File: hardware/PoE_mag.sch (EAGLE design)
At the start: 124 parts, among them IC1 LD1117V33, IC10 74LVC1T45SOT23-HAND, IC11 PCA9517A, IC2 LD1117V33, IC3 DS1338, IC4 ATMEGA1284, IC5 TSR 1-2450, IC6 MCP2200, IC7 74LVC1T45SOT23-HAND, IC8 74LVC1T45SOT23-HAND, IC9 74LVC1T45SOT23-HAND, Q1 BSS138, Q2 BUK98150-55A, X1 PWR, X2 JTAG, X3 USB, X4 MICRO-SD-SOCKETHIROSE-DM3D, X5 CONN-SMATHD, X6 UFL, X7 22-23-2021, X8 RJ45, X9 RJ11, Y1 32k768, Y2 16MHz, Y3 12MHz

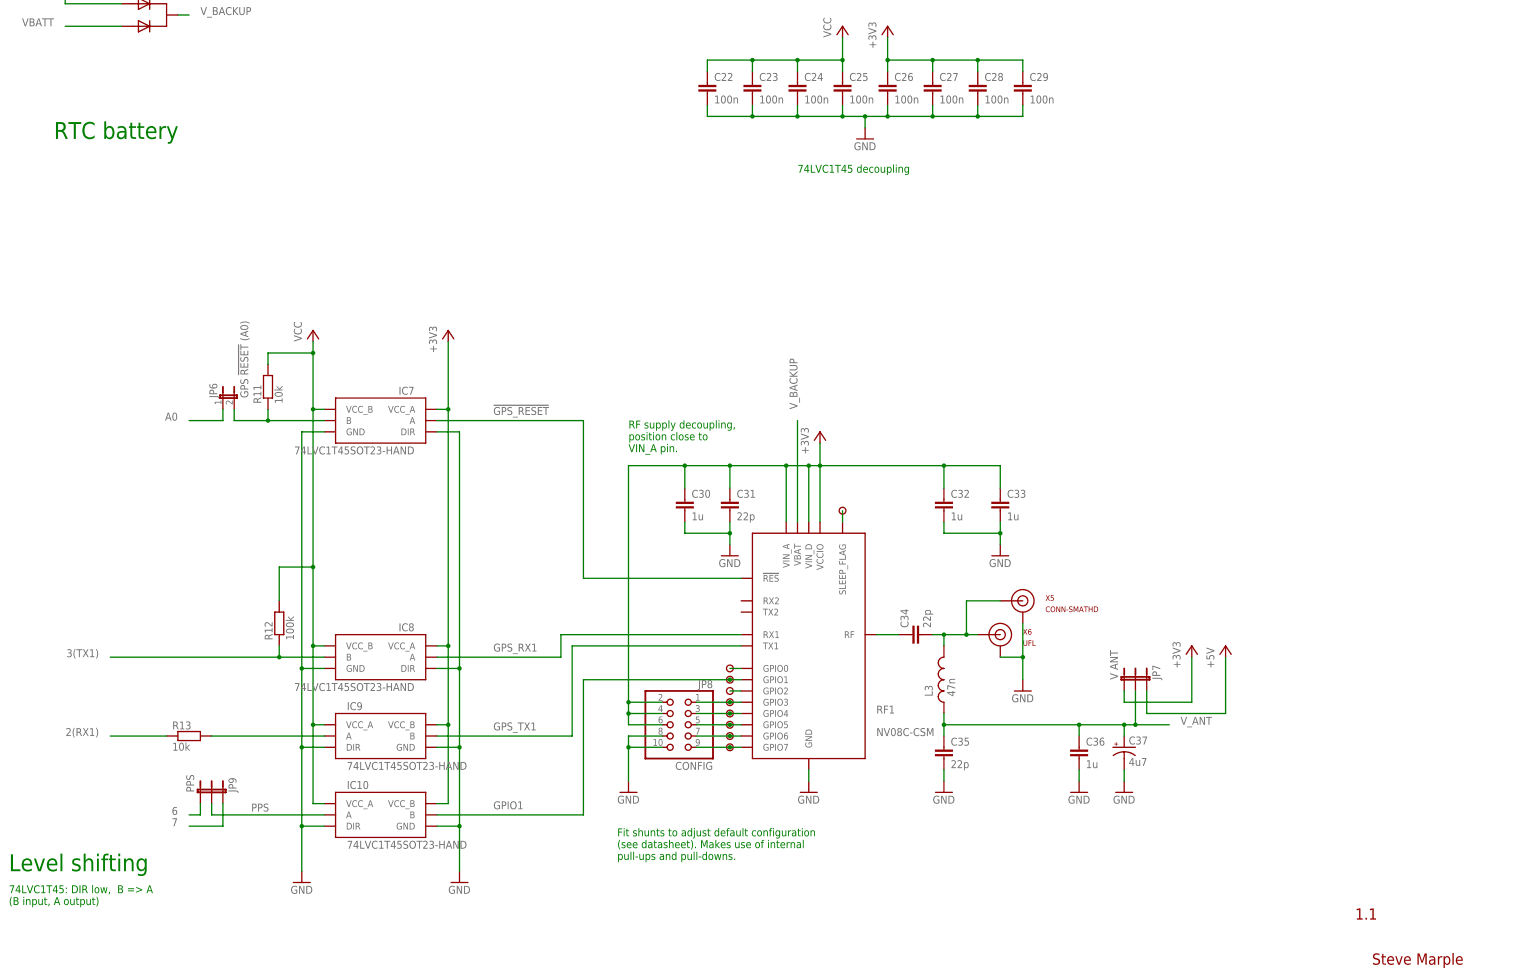
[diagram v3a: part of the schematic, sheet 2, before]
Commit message: Minor changes for ground pour
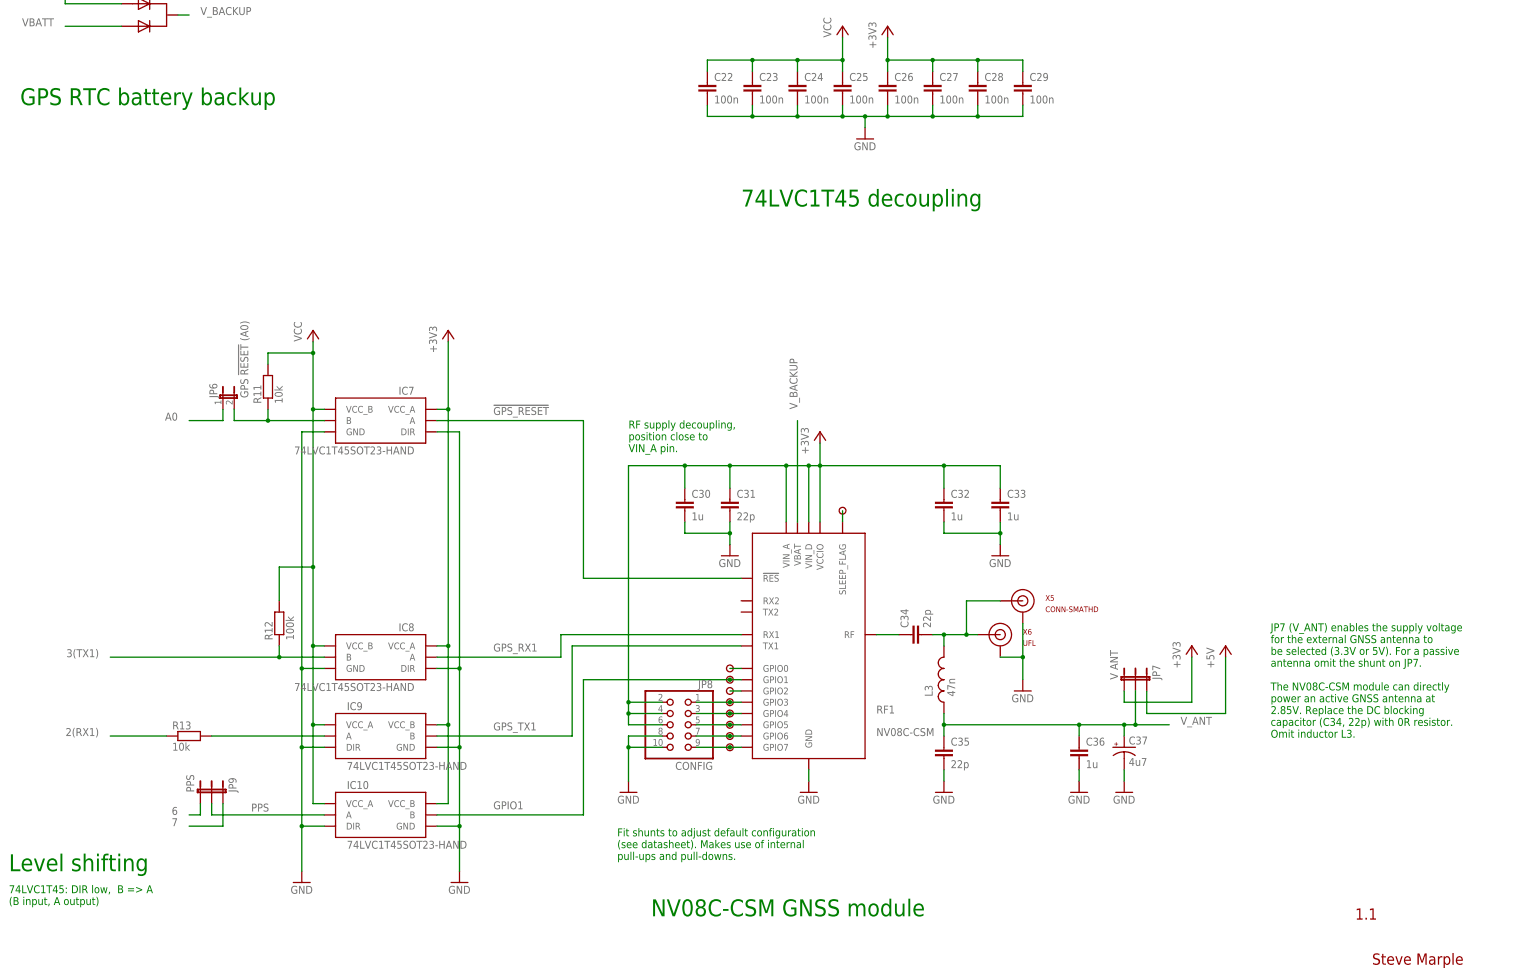
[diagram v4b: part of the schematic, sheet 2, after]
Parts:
- R14, R15, R16, R17: value 10k -> 4k7
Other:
- note added: "GPS RTC battery backup"
- note added: "JP7 (V_ANT) enables the supply voltage for the external GNSS antenna to be selected (3.3V or 5V). For a passive antenna omit the shunt on JP7. The NV08C-CSM module can directly power an active GNSS antenna at 2.85V. Replace the DC blocking capacitor (C34, 22p) with 0R resistor. Omit inductor L3."
- note added: "NV08C-CSM GNSS module"
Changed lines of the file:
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@@
 <part name="JP11" library="SparkFun" deviceset="JUMPER-3" device="PTH" value="MAG VCC"/>
 <part name="IC11" library="SteveMarple" deviceset="PCA9517A" device="SOIC" value="PCA9517A"/>
-<part name="R15" library="SteveMarple" deviceset="RESISTOR" device="1206-HAND" value="10k"/>
+<part name="R15" library="SteveMarple" deviceset="RESISTOR" device="1206-HAND" value="4k7"/>
 <part name="GND43" library="supply1" deviceset="GND" device=""/>
 <part name="P+18" library="supply1" deviceset="VCC" device=""/>
-<part name="R14" library="SteveMarple" deviceset="RESISTOR" device="1206-HAND" value="10k"/>
-<part name="R16" library="SteveMarple" deviceset="RESISTOR" device="1206-HAND" value="10k"/>
-<part name="R17" library="SteveMarple" deviceset="RESISTOR" device="1206-HAND" value="10k"/>
+<part name="R14" library="SteveMarple" deviceset="RESISTOR" device="1206-HAND" value="4k7"/>
+<part name="R16" library="SteveMarple" deviceset="RESISTOR" device="1206-HAND" value="4k7"/>
+<part name="R17" library="SteveMarple" deviceset="RESISTOR" device="1206-HAND" value="4k7"/>
 <part name="R20" library="SteveMarple" deviceset="RESISTOR" device="1206-HAND" value="3k 1%"/>
 <part name="R21" library="SteveMarple" deviceset="RESISTOR" device="1206-HAND" value="1k 1%"/>
@@
 <text x="332.74" y="4.318" size="2.54" layer="94">Steve Marple</text>
 <text x="25.4" y="25.4" size="3.81" layer="91" ratio="10">Level shifting</text>
-<text x="35.56" y="190.5" size="3.81" layer="91" ratio="10">RTC battery</text>
+<text x="27.94" y="198.12" size="3.81" layer="91" ratio="10">GPS RTC battery backup</text>
 <text x="25.4" y="17.78" size="1.778" layer="91">74LVC1T45: DIR low,  B =&gt; A
 (B input, A output)</text>
@@
 (see datasheet). Makes use of internal
 pull-ups and pull-downs.</text>
-<text x="203.2" y="182.88" size="1.778" layer="91">74LVC1T45 decoupling</text>
+<text x="190.5" y="175.26" size="3.81" layer="91" ratio="10">74LVC1T45 decoupling</text>
+<text x="170.18" y="15.24" size="3.81" layer="91" ratio="10">NV08C-CSM GNSS module</text>
+<text x="309.88" y="81.28" size="1.778" layer="91" align="top-left">JP7 (V_ANT) enables the supply voltage
+for the external GNSS antenna to
+be selected (3.3V or 5V). For a passive
+antenna omit the shunt on JP7.
+The NV08C-CSM module can directly
+power an active GNSS antenna at
+2.85V. Replace the DC blocking
+capacitor (C34, 22p) with 0R resistor.
+Omit inductor L3.</text>
 </plain>
 <instances>

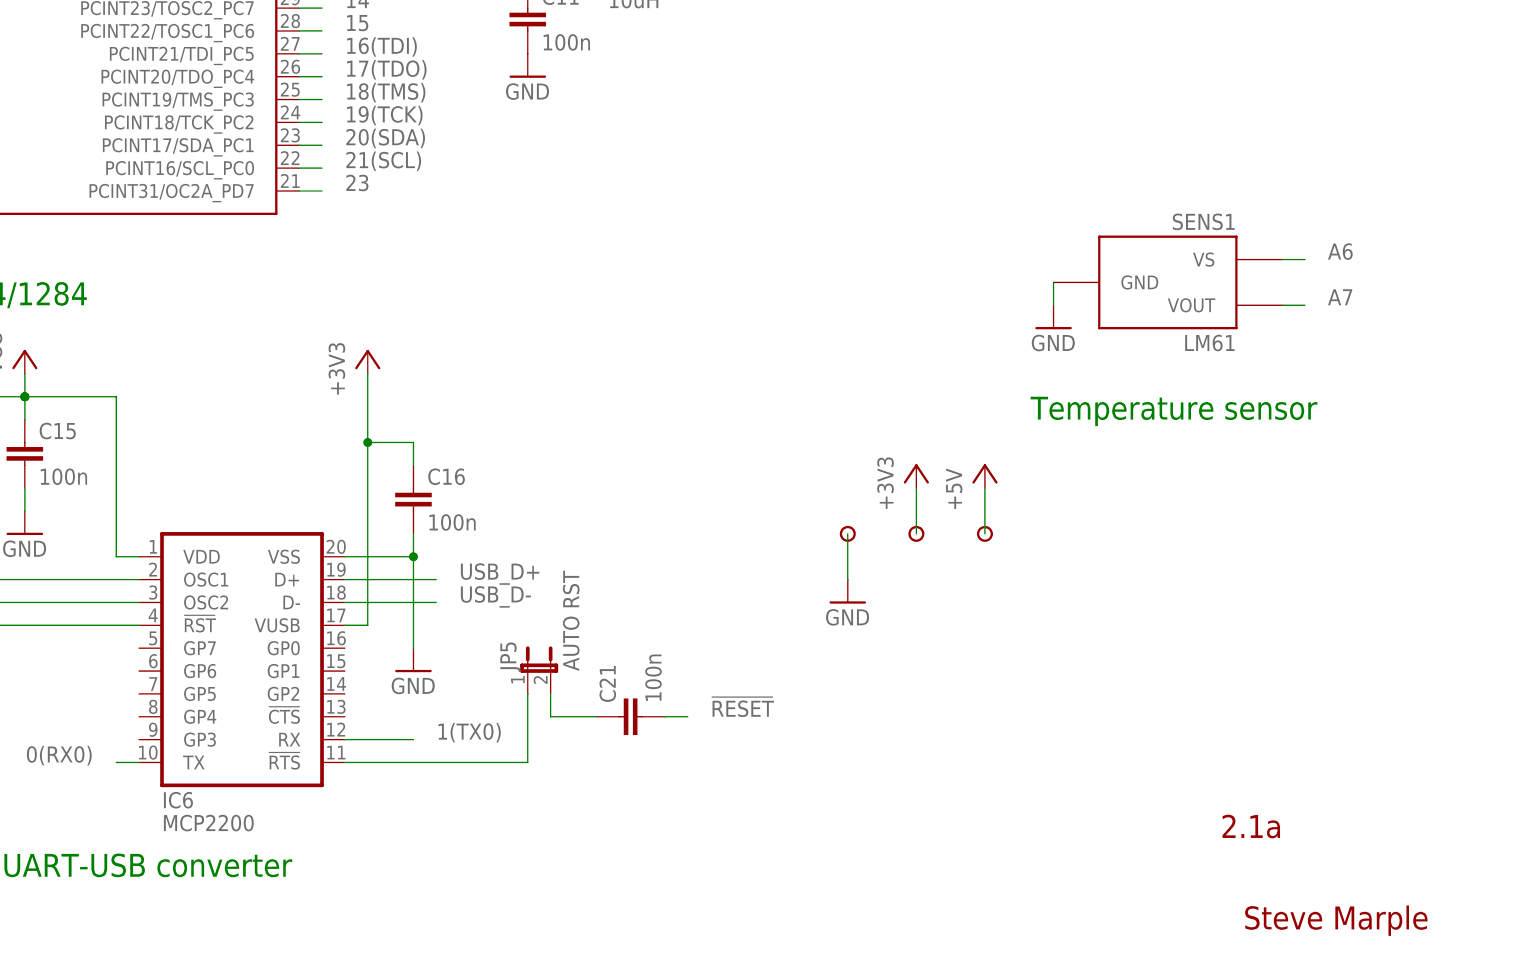
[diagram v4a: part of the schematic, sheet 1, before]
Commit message: Always power LM61 and swap to SOT23 package
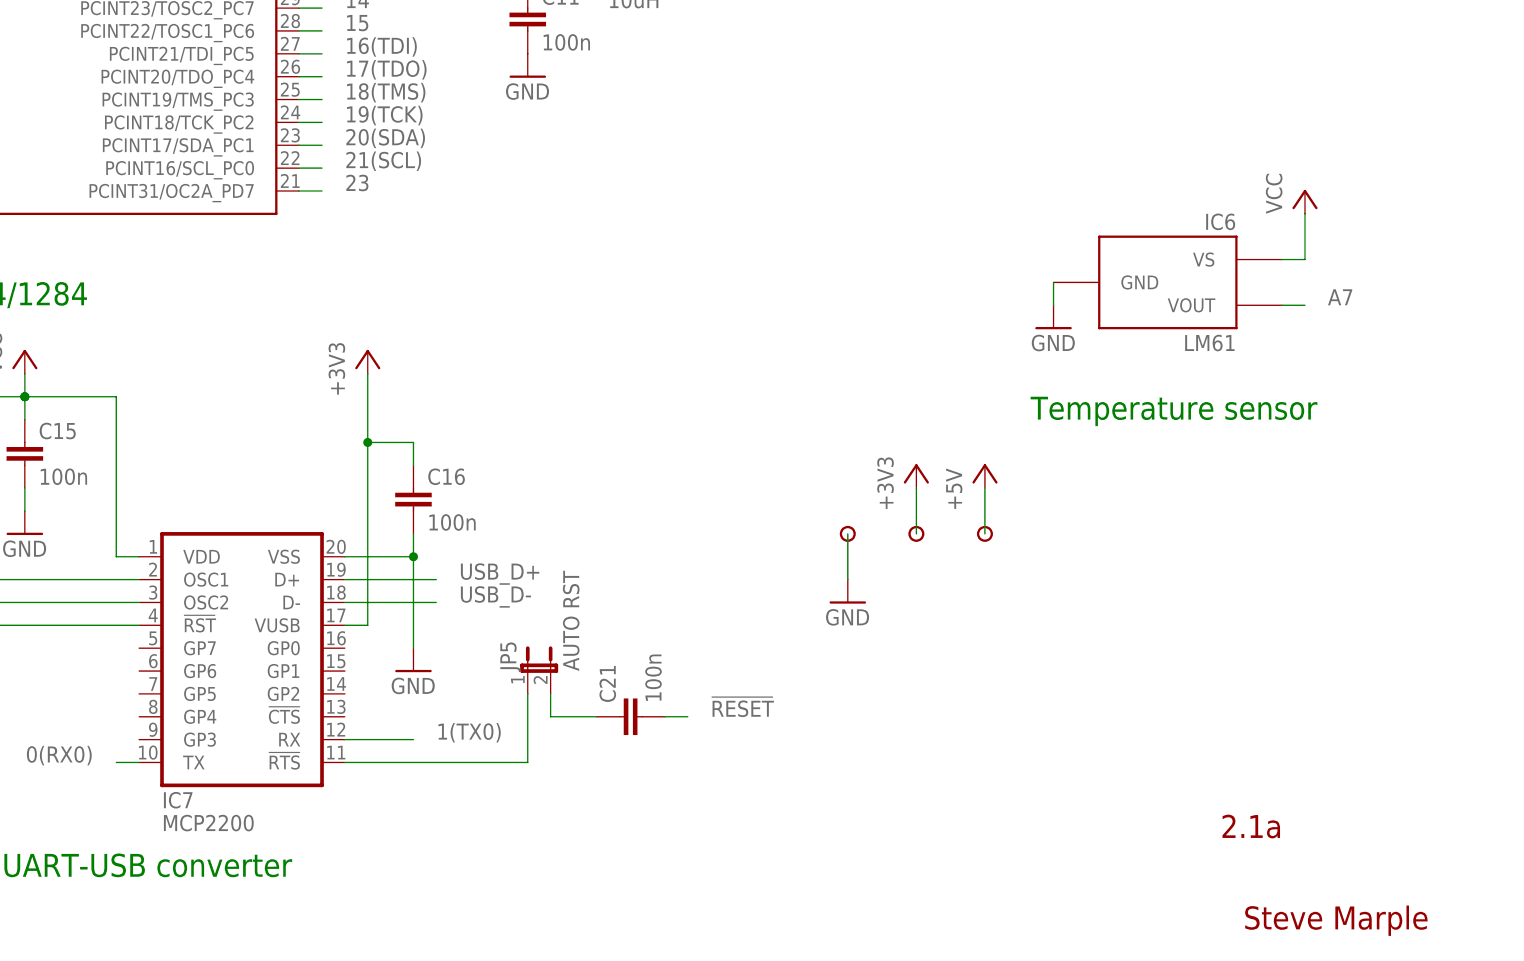
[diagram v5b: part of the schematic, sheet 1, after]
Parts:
- removed SENS1: LM61, SteveMarple:LM61
- added IC12: PCA9517A, SteveMarple:PCA9517ASOIC
- IC11: value PCA9517A -> 74LVC1T45SOT23-HAND; device SteveMarple:PCA9517ASOIC -> SteveMarple:74LVC1T45SOT23-HAND
- IC6: value MCP2200 -> LM61; device SteveMarple:MCP2200 -> SteveMarple:LM61SOT23
- IC7: value 74LVC1T45SOT23-HAND -> MCP2200; device SteveMarple:74LVC1T45SOT23-HAND -> SteveMarple:MCP2200
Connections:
- net !GPS_RESET: now also IC8.A; no longer IC7.A
- net !MCP2200_RESET: now also IC7.!RST; no longer IC6.!RST
- net +3V3: now also IC11.VCC_B, IC7.VUSB, IC9.VCC_A; no longer IC6.VUSB, IC7.VCC_A, IC9.VCC_B
- net 0(RX0): now also IC7.TX; no longer IC6.TX
- net 1(TX0): now also IC7.RX; no longer IC6.RX
- net 20(SDA): now also IC12.SDA_A; no longer IC11.SDA_A
- net 21(SCL): now also IC12.SCL_A; no longer IC11.SCL_A
- net 3(TX1): now also IC9.B; no longer IC8.B
- net A6: no longer SENS1.VS
- net A7: now also IC6.VOUT; no longer SENS1.VOUT
- net AUTO_RESET: now also IC7.!RTS; no longer IC6.!RTS
- net GND: now also IC11.DIR, IC12.GND, IC6.GND, IC7.VSS; no longer IC6.VSS, IC7.DIR, IC7.GND, SENS1.GND
- net GPIO1: now also IC11.B; no longer IC10.B
- net GPS_RX1: now also IC9.A; no longer IC8.A
- net GPS_TX1: now also IC10.B; no longer IC9.B
- net MAG_SCL: now also IC12.SCL_B; no longer IC11.SCL_B
- net MAG_SDA: now also IC12.SDA_B; no longer IC11.SDA_B
- net MAG_VCC: now also IC12.EN, IC12.VCC_B; no longer IC11.EN, IC11.VCC_B
- net N$18: now also IC7.OSC1; no longer IC6.OSC1
- net N$22: now also IC8.B; no longer IC7.B
- net N$25: now also IC10.A; no longer IC9.A
- net N$7: now also IC7.OSC2; no longer IC6.OSC2
- net PPS: now also IC11.A; no longer IC10.A
- net USB_D+: now also IC7.D+; no longer IC6.D+
- net USB_D-: now also IC7.D-; no longer IC6.D-
- net VCC: now also IC12.VCC_A, IC6.VS, IC7.VDD, IC9.VCC_B; no longer IC6.VDD, IC7.VCC_B, IC9.VCC_A
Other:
- moved on the sheet: IC10, IC8, IC9
